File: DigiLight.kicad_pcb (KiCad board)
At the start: 2 copper layers, 95 x 70 mm, 85 parts, among them IC1 MAX9814 Module, J1 IN_1, J2 IN_2, J3 POWER (5V/3A), J4 APU-2, J5 112J-TDAR-R-Micro_SD_Card, J6 WS2811, Q1 BC846, Q2 BC846, Q3 IRLML6402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

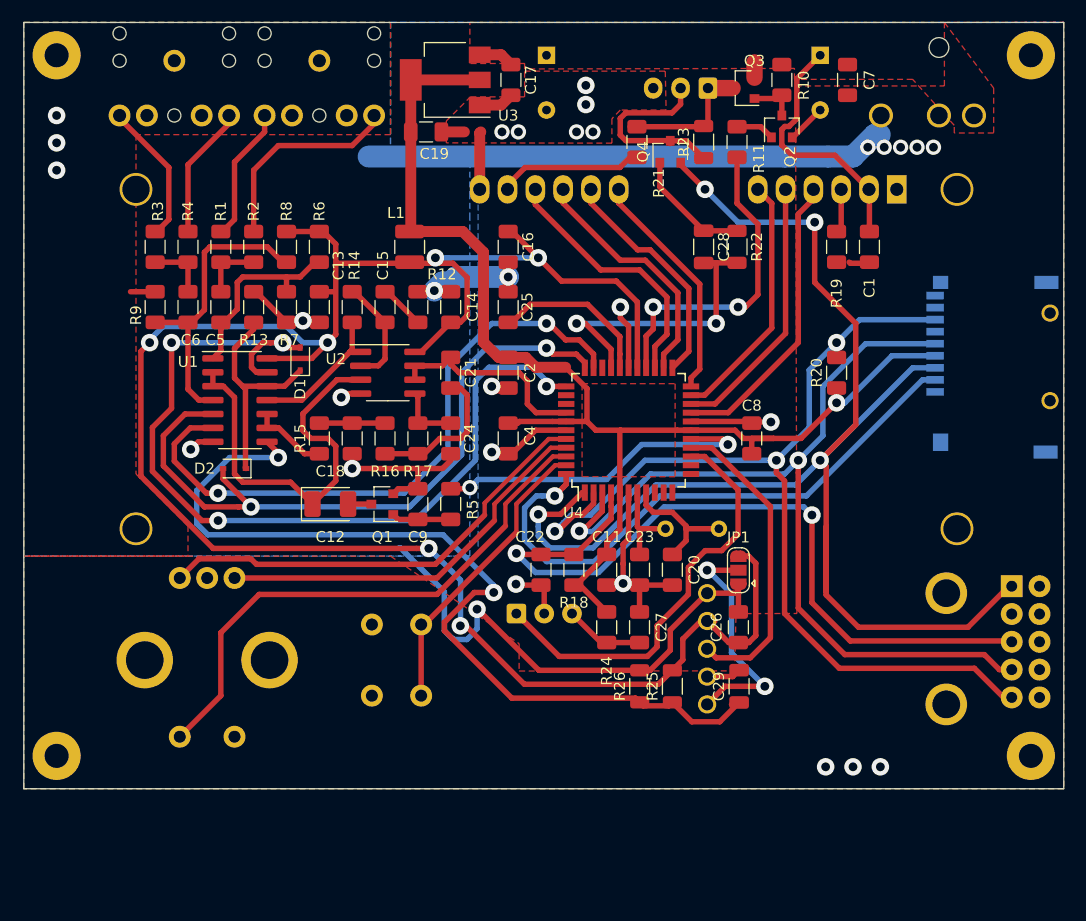
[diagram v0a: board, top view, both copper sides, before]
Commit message: Changed output switch on schematic and pcb
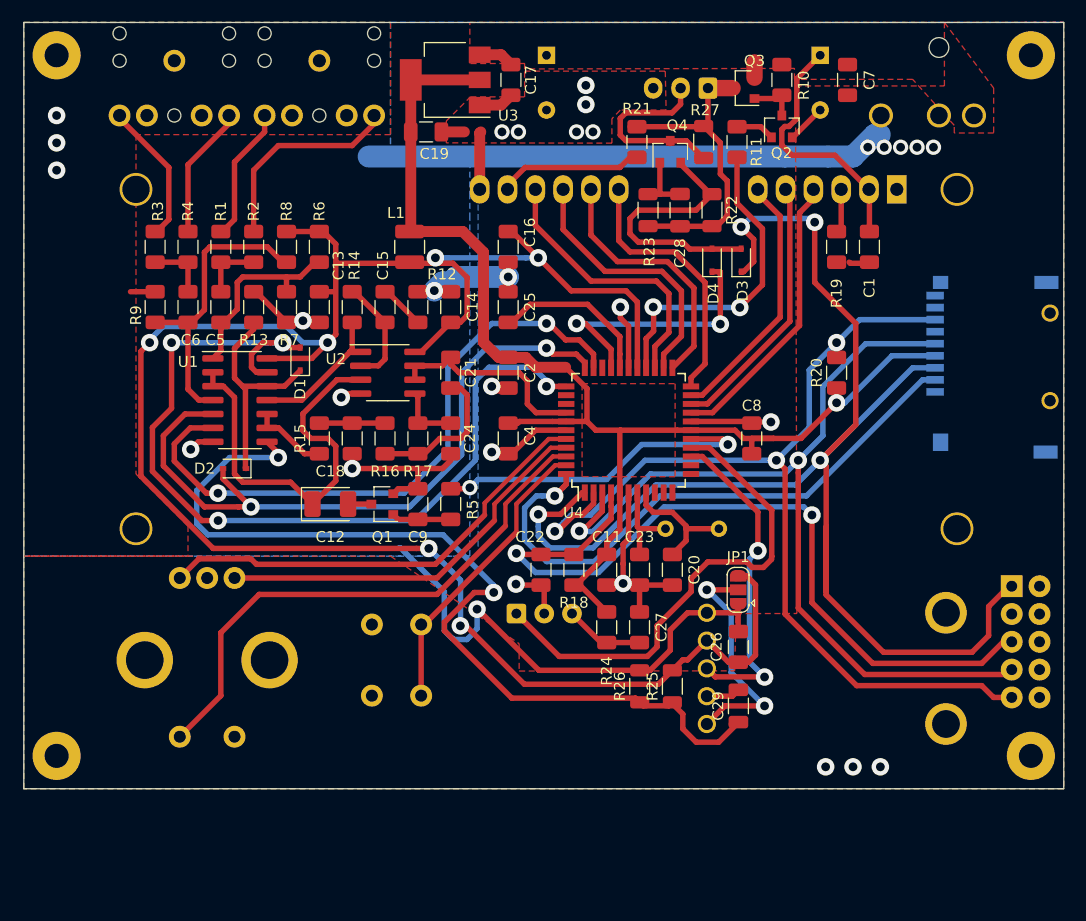
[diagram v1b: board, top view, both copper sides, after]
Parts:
- added D3: 1N4148WS, Diode_SMD:D_SOD-323, F.Cu at (212.5, 75.7)
- added D4: 1N4148WS, Diode_SMD:D_SOD-323, F.Cu at (209.9, 75.7)
- added R23: 10K, Resistor_SMD:R_1206_3216Metric, F.Cu at (204.0, 71.1)
- moved R22 4.06 mm to (209.9, 71.1)
- moved C28 3.99 mm to (206.9, 71.1)
- moved C29 1.79 mm to (212.3, 116.4)
- moved JP1 1.79 mm to (212.3, 105.8)
- moved IC1 1.79 mm to (233.3, 113.0)
- moved C26 1.79 mm to (212.3, 111.0)
- renumbered R23 to R27
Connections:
- C28 pad 2: /WS_LOCK -> VPP
- Q4 pad 2: /MOSI -> Net-(D3-Pad2)
- R22 pad 1: Net-(C28-Pad1) -> Net-(D3-Pad2)
- R22 pad 2: /WS_LOCK -> VPP
- U4 pad 14: /IR -> /MC_GAIN
- U4 pad 15: /MC_GAIN -> /IR
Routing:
- net Net-(D3-Pad2): track 0.00 -> 24.8 mm
- net VPP: track 12.5 -> 29.3 mm
- net /IR: track 38.7 -> 45.1 mm
- net Net-(C28-Pad1): track 10.9 -> 5.67 mm
- net /WS_LOCK: track 28.3 -> 24.5 mm
- net /LCD_D0: track 21.4 -> 24.2 mm
- net /LCD_D1: track 21.3 -> 23.7 mm
- net /LCD_D2: track 22.5 -> 24.5 mm
- net VDDA: track 184.9 -> 183.2 mm
- net Net-(C29-Pad1): track 81.5 -> 83.2 mm
- net /RESET: track 70.7 -> 72.3 mm
- net /LCD_D3: track 23.8 -> 25.4 mm
- net /MC_GAIN: track 28.3 -> 29.8 mm, vias 0 -> 2
- net /MOSI: track 128.1 -> 129.3 mm
- net /LCD_RS: track 27.0 -> 26.2 mm
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
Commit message: Changed the contour of the PCB
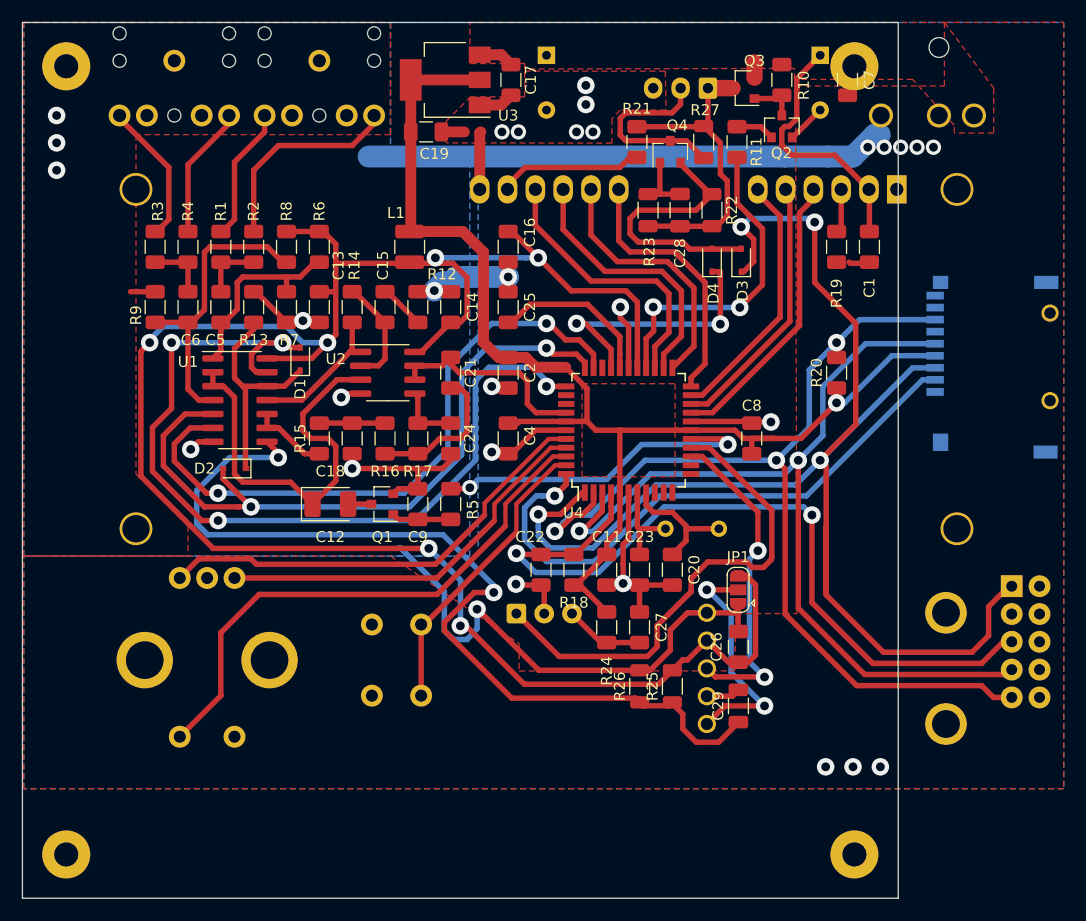
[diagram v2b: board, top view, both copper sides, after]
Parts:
- moved REF** 18.5 mm to (222.9, 130.0)
- moved REF** 16.2 mm to (222.9, 58.0)
- moved REF** 9.05 mm to (150.9, 130.0)
- moved REF** 1.33 mm to (150.9, 58.0)
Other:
- board size 95 x 70 mm -> 80 x 80 mm
